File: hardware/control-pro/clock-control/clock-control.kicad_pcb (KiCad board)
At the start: 2 copper layers, 100 x 90 mm, 19 parts, among them J1 OUTPUT, J2 INPUT, SW1 CLOCK_SPEED, SW2 CLOCK_STEP

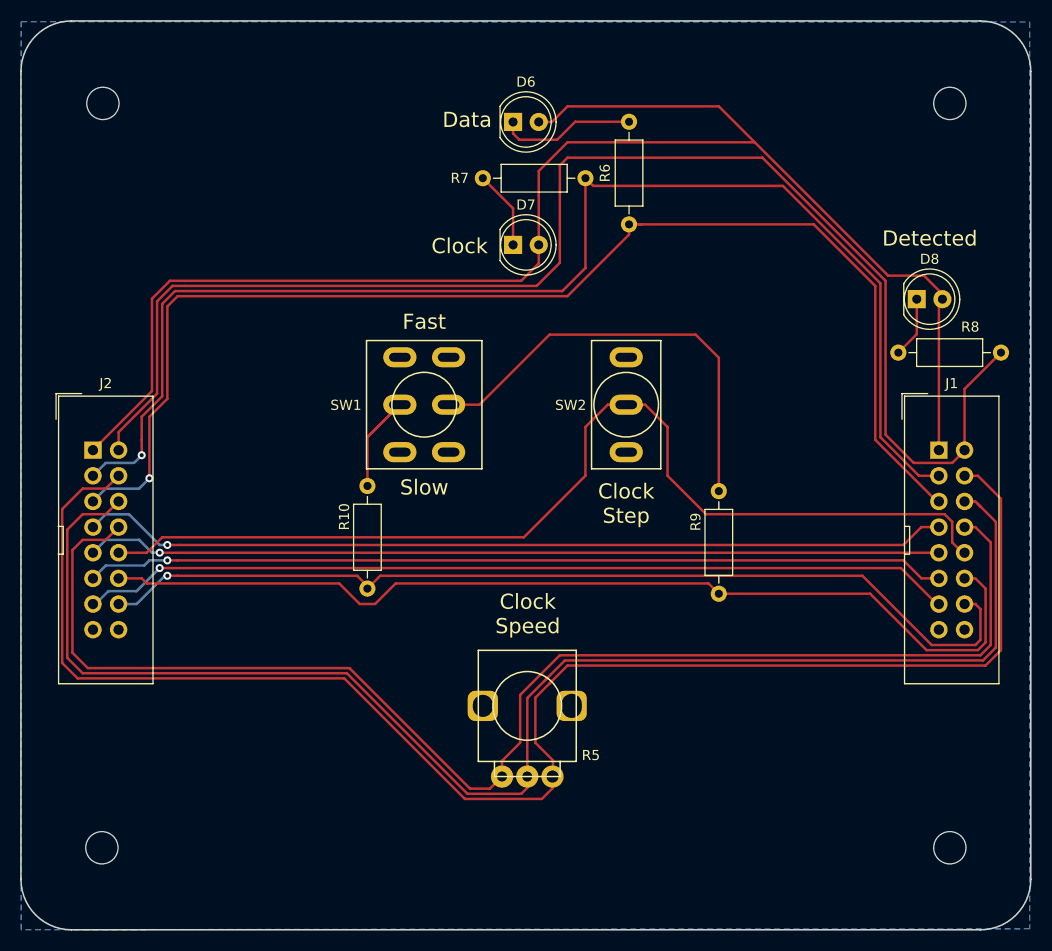
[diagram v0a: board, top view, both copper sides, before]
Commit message: TX2: - Added buffer to drive LEDs - Added decoupling capacitors - Fixed dimmer traces on PCB
DMX-CPC*:
- Switched to horizontal 16 pin connectors since vertical was too tall with a cable plugged in
- Swapped the clock speed and step switches to match the order on the TX1
- Swapped the data and clock LEDs to match the order on the TX1

DMX-CPD*:
- Split dimmer controls out to its own PCB
- Added 2nd 16 pin connector to daisy chain with DMX-CPC*.
- Switched to horizontal 16 pin connectors since vertical was too tall with a cable plugged in

Updated readmes with parts, board links.
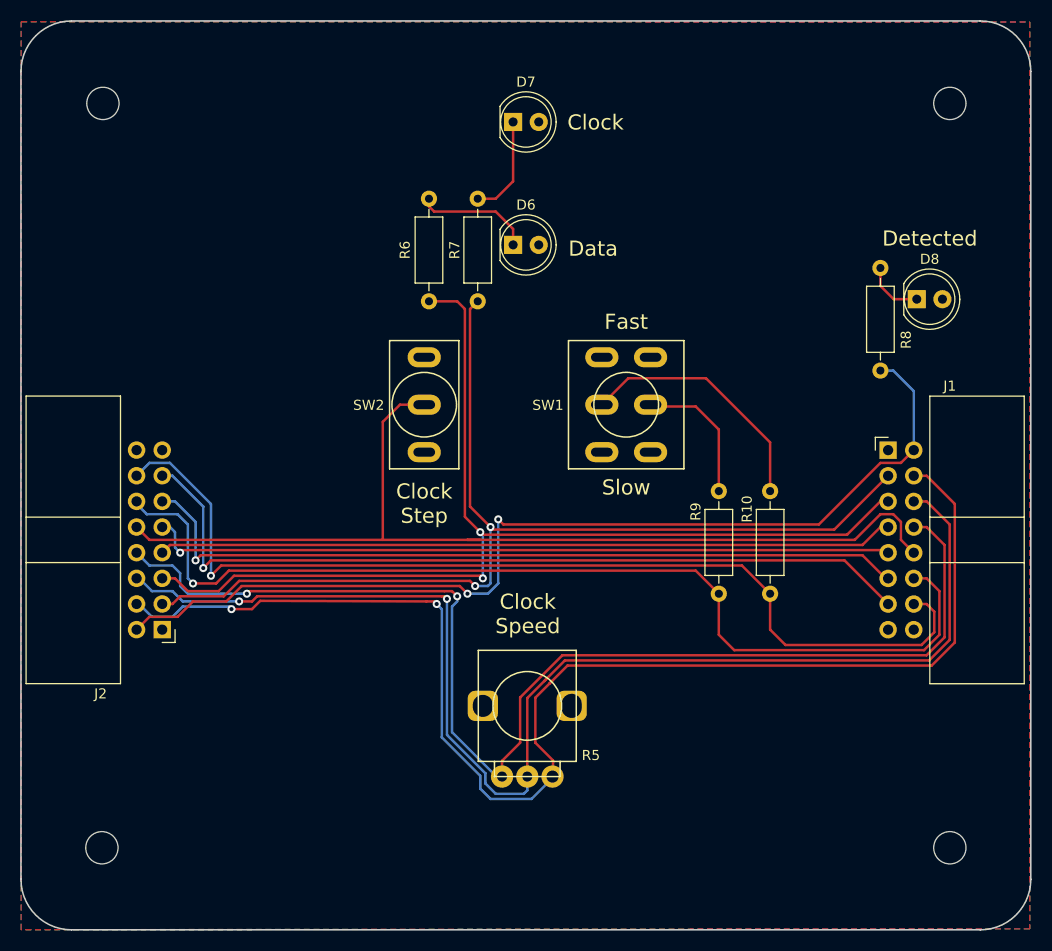
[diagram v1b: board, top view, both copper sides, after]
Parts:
- removed the ? at (171.7, 135.9)
- added ?: , footprints:OSHW-LOGO-S, B.Cu at (171.7, 135.8)
- J1, J2: footprint Connector_IDC:IDC-Header_2x08_P2.54mm_Vertical -> Connector_IDC:IDC-Header_2x08_P2.54mm_Horizontal
- moved R10 39.9 mm to (161.3, 105.4)
- moved R6 21.2 mm to (127.5, 76.5)
- moved SW1 20.0 mm to (147.0, 86.7)
- moved SW2 20.0 mm to (127.0, 86.7)
- moved J2 19.1 mm to (101.1, 109.0), turned to 180 degrees
- moved R7 16.2 mm to (132.3, 76.5), turned to 90 degrees
- moved D6 12.2 mm to (135.8, 70.9)
- moved D7 12.2 mm to (135.8, 58.7)
- moved R8 12.1 mm to (172.2, 83.3), turned to 90 degrees
- moved J1 5.03 mm to (173.0, 91.2)
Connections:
- net /ACTIVE renamed /~HWD_DT
- net /ADJ_1 renamed /SPD_LO
- net /ADJ_2 renamed /SPD_WIPER
- net /ADJ_3 renamed /SPD_HI
- net /CLOCK renamed /~CLOCK
- net /DATA renamed /~DATA
- net /FAST renamed /~CLK_FST
- net /SLOW renamed /~CLK_SLO
- net /STEP renamed /~CLK_STEP
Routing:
- net +5V: track 153.4 -> 0.58 mm
- net /~HWD_DT: track 141.0 -> 99.1 mm, vias 0 -> 2
- net Net-(R9-Pad2): track 43.8 -> 13.9 mm
- net /~CLOCK: track 129.9 -> 104.6 mm, vias 1 -> 2
- net /SPD_HI: track 154.5 -> 131.5 mm, vias 0 -> 2
- net /~DATA: track 125.2 -> 106.2 mm, vias 1 -> 2
- net /SPD_WIPER: track 144.9 -> 126.3 mm, vias 0 -> 2
- net /SPD_LO: track 135.1 -> 120.9 mm, vias 0 -> 2
- net /DIM1: track 86.3 -> 72.9 mm, vias 1 -> 0
- net Net-(R10-Pad2): track 13.9 -> 25.2 mm
- net /DIM2: track 84.8 -> 74.0 mm
- net /DIM3: track 85.3 -> 77.7 mm
- net /DIM4: track 86.7 -> 81.4 mm
- net /~CLK_STEP: track 102.8 -> 98.9 mm
- net /~CLK_FST: track 95.6 -> 99.0 mm
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- added copper zone on F.Cu, net +5V
